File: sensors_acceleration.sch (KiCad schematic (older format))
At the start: 5 parts

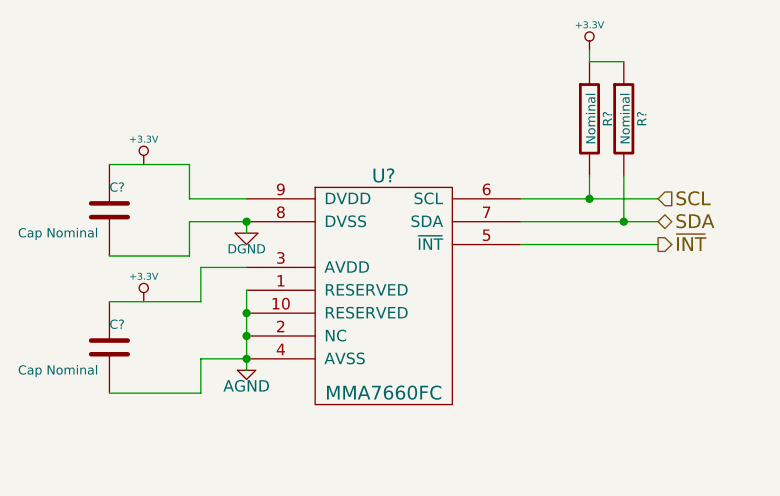
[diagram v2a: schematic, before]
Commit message: various fixes due to issues found in ERC
learned how to use invisible pins
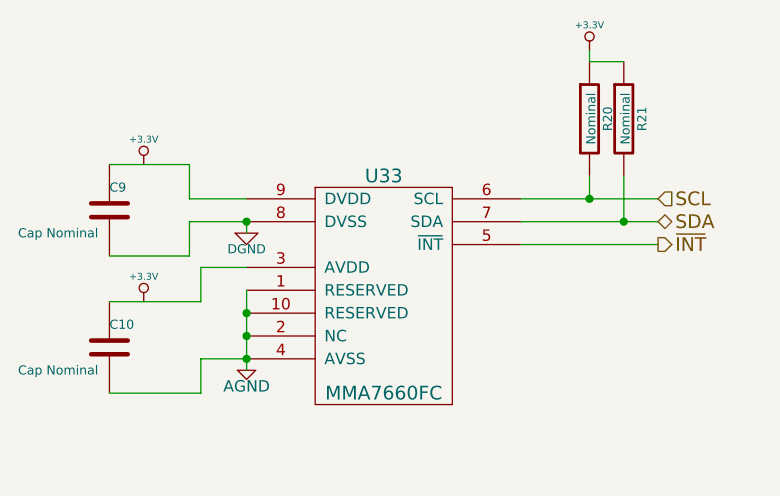
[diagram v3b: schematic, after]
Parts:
- gave numbers to parts that had none: 5
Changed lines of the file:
@@
 Sheet 9 18
 Title ""
-Date "18 dec 2013"
+Date "20 dec 2013"
 Rev ""
 Comp ""
@@
 $EndDescr
 $Comp
-L MMA7660FC U?
+L MMA7660FC U33
 U 1 1 527C80D0
 P 2300 1200
-F 0 "U?" H 2300 1200 60  0000 C CNN
+F 0 "U33" H 2300 1200 60  0000 C CNN
 F 1 "MMA7660FC" H 2300 250 60  0000 C CNN
 F 2 "" H 2300 1200 60  0000 C CNN
@@
 $EndComp
 $Comp
-L R R?
+L R R20
 U 1 1 527C8316
 P 3200 950
-F 0 "R?" V 3280 950 40  0000 C CNN
+F 0 "R20" V 3280 950 40  0000 C CNN
 F 1 "Nominal" V 3207 951 40  0000 C CNN
 F 2 "~" V 3130 950 30  0000 C CNN
@@
 $EndComp
 $Comp
-L C C?
+L C C9
 U 1 1 527C831C
 P 1100 1350
-F 0 "C?" H 1100 1450 40  0000 L CNN
+F 0 "C9" H 1100 1450 40  0000 L CNN
 F 1 "Cap Nominal" H 700 1250 40  0000 L CNN
 F 2 "~" H 1138 1200 30  0000 C CNN
@@
 $EndComp
 $Comp
-L C C?
+L C C10
 U 1 1 527C8323
 P 1100 1950
-F 0 "C?" H 1100 2050 40  0000 L CNN
+F 0 "C10" H 1100 2050 40  0000 L CNN
 F 1 "Cap Nominal" H 700 1850 40  0000 L CNN
 F 2 "~" H 1138 1800 30  0000 C CNN
@@
 $EndComp
 $Comp
-L +3.3V #PWR?
+L +3.3V #PWR045
 U 1 1 527C8347
 P 1250 1150
-F 0 "#PWR?" H 1250 1110 30  0001 C CNN
+F 0 "#PWR045" H 1250 1110 30  0001 C CNN
 F 1 "+3.3V" H 1250 1260 30  0000 C CNN
 F 2 "" H 1250 1150 60  0000 C CNN
@@
 $EndComp
 $Comp
-L DGND #PWR?
+L DGND #PWR046
 U 1 1 527C8356
 P 1700 1450
-F 0 "#PWR?" H 1700 1450 40  0001 C CNN
+F 0 "#PWR046" H 1700 1450 40  0001 C CNN
 F 1 "DGND" H 1700 1380 40  0000 C CNN
 F 2 "" H 1700 1450 60  0000 C CNN
@@
 $EndComp
 $Comp
-L AGND #PWR?
+L AGND #PWR047
 U 1 1 527C83EE
 P 1700 2050
-F 0 "#PWR?" H 1700 2050 40  0001 C CNN
+F 0 "#PWR047" H 1700 2050 40  0001 C CNN
 F 1 "AGND" H 1700 1980 50  0000 C CNN
 F 2 "" H 1700 2050 60  0000 C CNN
@@
 $EndComp
 $Comp
-L +3.3V #PWR?
+L +3.3V #PWR048
 U 1 1 527C8426
 P 1250 1750
-F 0 "#PWR?" H 1250 1710 30  0001 C CNN
+F 0 "#PWR048" H 1250 1710 30  0001 C CNN
 F 1 "+3.3V" H 1250 1860 30  0000 C CNN
 F 2 "" H 1250 1750 60  0000 C CNN
@@
 $EndComp
 $Comp
-L R R?
+L R R21
 U 1 1 527C8433
 P 3350 950
-F 0 "R?" V 3430 950 40  0000 C CNN
+F 0 "R21" V 3430 950 40  0000 C CNN
 F 1 "Nominal" V 3357 951 40  0000 C CNN
 F 2 "~" V 3280 950 30  0000 C CNN
@@
 ~INT
 $Comp
-L +3.3V #PWR?
+L +3.3V #PWR049
 U 1 1 527C85AB
 P 3200 650
-F 0 "#PWR?" H 3200 610 30  0001 C CNN
+F 0 "#PWR049" H 3200 610 30  0001 C CNN
 F 1 "+3.3V" H 3200 760 30  0000 C CNN
 F 2 "" H 3200 650 60  0000 C CNN

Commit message: started figuring out how to get pcb going
also need to figure out how to make some footprints, although there is a
nice library of footprints avalible already
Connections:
- net DGND is gone; now on net AGND: C9.2, U33.8 (DVSS)
- net +3.3V: now also C10.1, C9.1, U33.3 (AVDD), U33.9 (DVDD)
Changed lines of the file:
@@
 Sheet 9 18
 Title ""
-Date "20 dec 2013"
+Date "21 dec 2013"
 Rev ""
 Comp ""
@@
 Connection ~ 1700 1400
 Wire Wire Line
-	1500 2000 1700 2000
-Wire Wire Line
-	1500 2150 1500 2000
-Wire Wire Line
-	1100 2150 1500 2150
+	1700 2000 1500 2000
+Wire Wire Line
+	1500 2000 1500 2150
+Wire Wire Line
+	1500 2150 1100 2150
 Connection ~ 1700 2000
 Connection ~ 1700 1900
@@
 Wire Wire Line
 	3200 700  3350 700
+Connection ~ 1250 1150
+Connection ~ 1250 1750
+$Comp
+L DGND #PWR050
+U 1 1 52B5F4D4
+P 1400 2400
+F 0 "#PWR050" H 1400 2400 40  0001 C CNN
+F 1 "DGND" H 1400 2330 40  0000 C CNN
+F 2 "" H 1400 2400 60  0000 C CNN
+F 3 "" H 1400 2400 60  0000 C CNN
+	1    1400 2400
+	1    0    0    -1
+$EndComp
+$Comp
+L AGND #PWR051
+U 1 1 52B5F4DA
+P 1600 2400
+F 0 "#PWR051" H 1600 2400 40  0001 C CNN
+F 1 "AGND" H 1600 2330 50  0000 C CNN
+F 2 "" H 1600 2400 60  0000 C CNN
+F 3 "" H 1600 2400 60  0000 C CNN
+	1    1600 2400
+	1    0    0    -1
+$EndComp
+Wire Wire Line
+	1400 2400 1400 2350
+Wire Wire Line
+	1400 2350 1600 2350
+Wire Wire Line
+	1600 2350 1600 2400
 $EndSCHEMATC

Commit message: placed components ... quite the task!
there is a lot of shit going on in this board... :D
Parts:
- renumbered C9 to C6, C10 to C7, U33 to U32
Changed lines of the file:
@@
 $Descr A4 11693 8268
 encoding utf-8
-Sheet 9 18
+Sheet 9 15
 Title ""
-Date "12 jan 2014"
+Date "18 jan 2014"
 Rev ""
 Comp ""
@@
 $EndDescr
 $Comp
-L MMA7660FC U33
+L MMA7660FC U32
 U 1 1 527C80D0
 P 2300 1200
-F 0 "U33" H 2300 1200 60  0000 C CNN
+F 0 "U32" H 2300 1200 60  0000 C CNN
 F 1 "MMA7660FC" H 2300 250 60  0000 C CNN
 F 2 "" H 2300 1200 60  0000 C CNN
@@
 $EndComp
 $Comp
-L C C9
+L C C6
 U 1 1 527C831C
 P 1100 1350
-F 0 "C9" H 1100 1450 40  0000 L CNN
+F 0 "C6" H 1100 1450 40  0000 L CNN
 F 1 "Cap Nominal" H 700 1250 40  0000 L CNN
 F 2 "~" H 1138 1200 30  0000 C CNN
@@
 $EndComp
 $Comp
-L C C10
+L C C7
 U 1 1 527C8323
 P 1100 1950
-F 0 "C10" H 1100 2050 40  0000 L CNN
+F 0 "C7" H 1100 2050 40  0000 L CNN
 F 1 "Cap Nominal" H 700 1850 40  0000 L CNN
 F 2 "~" H 1138 1800 30  0000 C CNN
@@
 $EndComp
 $Comp
-L +3.3V #PWR045
+L +3.3V #PWR040
 U 1 1 527C8347
 P 1250 1150
-F 0 "#PWR045" H 1250 1110 30  0001 C CNN
+F 0 "#PWR040" H 1250 1110 30  0001 C CNN
 F 1 "+3.3V" H 1250 1260 30  0000 C CNN
 F 2 "" H 1250 1150 60  0000 C CNN
@@
 $EndComp
 $Comp
-L DGND #PWR046
+L DGND #PWR041
 U 1 1 527C8356
 P 1700 1450
-F 0 "#PWR046" H 1700 1450 40  0001 C CNN
+F 0 "#PWR041" H 1700 1450 40  0001 C CNN
 F 1 "DGND" H 1700 1380 40  0000 C CNN
 F 2 "" H 1700 1450 60  0000 C CNN
@@
 $EndComp
 $Comp
-L AGND #PWR047
+L AGND #PWR042
 U 1 1 527C83EE
 P 1700 2050
-F 0 "#PWR047" H 1700 2050 40  0001 C CNN
+F 0 "#PWR042" H 1700 2050 40  0001 C CNN
 F 1 "AGND" H 1700 1980 50  0000 C CNN
 F 2 "" H 1700 2050 60  0000 C CNN
@@
 $EndComp
 $Comp
-L +3.3V #PWR048
+L +3.3V #PWR043
 U 1 1 527C8426
 P 1250 1750
-F 0 "#PWR048" H 1250 1710 30  0001 C CNN
+F 0 "#PWR043" H 1250 1710 30  0001 C CNN
 F 1 "+3.3V" H 1250 1860 30  0000 C CNN
 F 2 "" H 1250 1750 60  0000 C CNN
@@
 ~INT
 $Comp
-L +3.3V #PWR049
+L +3.3V #PWR044
 U 1 1 527C85AB
 P 3200 650
-F 0 "#PWR049" H 3200 610 30  0001 C CNN
+F 0 "#PWR044" H 3200 610 30  0001 C CNN
 F 1 "+3.3V" H 3200 760 30  0000 C CNN
 F 2 "" H 3200 650 60  0000 C CNN
@@
 Connection ~ 1250 1750
 $Comp
-L DGND #PWR050
+L DGND #PWR045
 U 1 1 52B5F4D4
 P 1400 2400
-F 0 "#PWR050" H 1400 2400 40  0001 C CNN
+F 0 "#PWR045" H 1400 2400 40  0001 C CNN
 F 1 "DGND" H 1400 2330 40  0000 C CNN
 F 2 "" H 1400 2400 60  0000 C CNN
@@
 $EndComp
 $Comp
-L AGND #PWR051
+L AGND #PWR046
 U 1 1 52B5F4DA
 P 1600 2400
-F 0 "#PWR051" H 1600 2400 40  0001 C CNN
+F 0 "#PWR046" H 1600 2400 40  0001 C CNN
 F 1 "AGND" H 1600 2330 50  0000 C CNN
 F 2 "" H 1600 2400 60  0000 C CNN
